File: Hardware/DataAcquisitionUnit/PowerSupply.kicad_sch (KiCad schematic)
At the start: 10 parts, among them U1 LM2901, U2 LD1117S50TR_SOT223

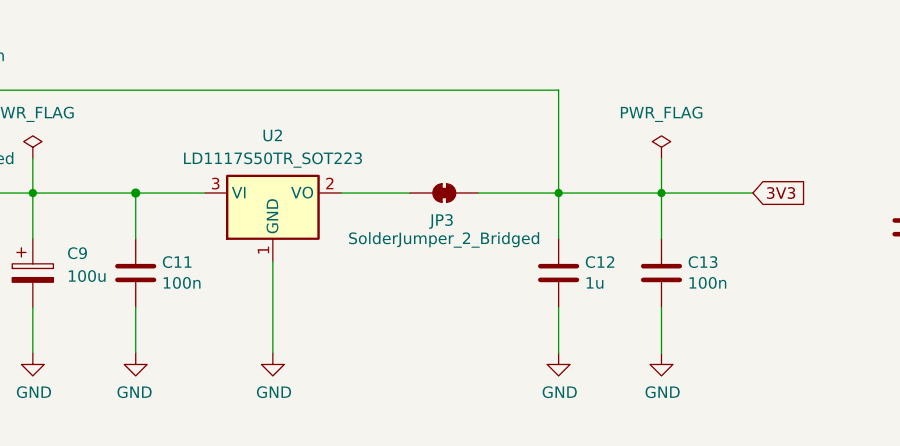
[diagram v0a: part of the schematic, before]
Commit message: rework CI, make PCB smaller
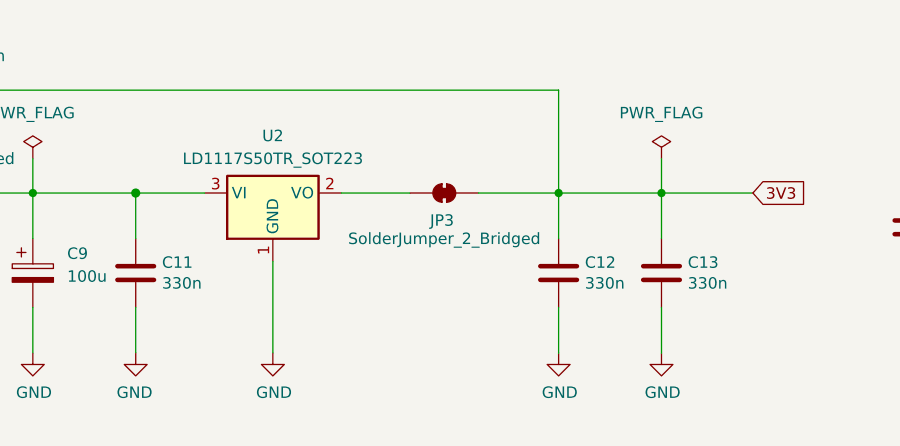
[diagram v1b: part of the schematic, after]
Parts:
- C11, C13: value 100n -> 330n
- C12: value 1u -> 330n
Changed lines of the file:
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@@
 			)
 		)
-		(property "Value" "1u"
+		(property "Value" "330n"
 			(at 156.591 105.283 0)
 			(effects
@@
 			)
 		)
-		(property "Value" "100n"
+		(property "Value" "330n"
 			(at 168.021 105.283 0)
 			(effects
@@
 			)
 		)
-		(property "Value" "100n"
+		(property "Value" "330n"
 			(at 109.601 105.283 0)
 			(effects
